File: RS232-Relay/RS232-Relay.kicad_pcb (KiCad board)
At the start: 2 copper layers, 82.5 x 151 mm, 133 parts, among them J10 Relay 1-4, J11 Relay 1-4, J2 Conn_01x02, J4 Conn_01x09, J5 Conn_01x09, J7 RS232_1, J8 RS232_2, J9 Relay 1-4, K1 G5V-1, K10 G5V-1, K11 G5V-1, K12 G5V-1, K2 G5V-1, K3 G5V-1, K4 G5V-1, K5 G5V-1, K6 G5V-1, K7 G5V-1, K8 G5V-1, K9 G5V-1, Q1 2N3904, Q10 2N3904, Q11 2N3904, Q12 2N3904, Q2 2N3904, Q3 2N3904, Q4 2N3904, Q5 2N3904, Q6 2N3904, Q7 2N3904, Q8 2N3904, Q9 2N3904, SW2 SW_SPST, SW3 SW_SPST, U1 TEC2-1210WI, U2 LTV-847S, U3 PCF8575DBR, U4 MAX3232, U6 LTV-847S, U7 LTV-847S

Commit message: 1x Layout Complete
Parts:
- removed D22, D23, D26, D27: 1N4148W, Diode_SMD:D_SOD-123
- removed D24, D25: RED, LED_SMD:LED_0805_2012Metric
- removed K10, K11, K12: G5V-1, Relay_THT:Relay_SPDT_Omron_G5V-1
- removed Q10, Q11, Q12: 2N3904, Package_TO_SOT_SMD:SOT-23
- removed R35, R40, R41: 220R, Resistor_SMD:R_0603_1608Metric
- removed R36, R37, R42, R43: 660R, Resistor_SMD:R_0603_1608Metric
- removed R38, R39: 1000R, Resistor_SMD:R_0603_1608Metric
- removed U7: LTV-847S, Package_DIP:SMDIP-16_W9.53mm
- added D28: RED, LED_SMD:LED_0805_2012Metric, F.Cu at (103.4, 39.6)
- added D29: 1N4148W, Diode_SMD:D_SOD-123, F.Cu at (103.0, 43.1)
- added D30: RED, LED_SMD:LED_0805_2012Metric, F.Cu at (53.7, 145.8)
- added D31: 1N4148W, Diode_SMD:D_SOD-123, F.Cu at (53.3, 149.3)
- added D32: RED, LED_SMD:LED_0805_2012Metric, F.Cu at (55.0, 92.4)
- added D33: 1N4148W, Diode_SMD:D_SOD-123, F.Cu at (54.6, 95.9)
- added K13: G5V-1, Relay_THT:Relay_SPDT_Omron_G5V-1, F.Cu at (99.9, 40.4)
- added K14: G5V-1, Relay_THT:Relay_SPDT_Omron_G5V-1, F.Cu at (50.2, 146.6)
- added K15: G5V-1, Relay_THT:Relay_SPDT_Omron_G5V-1, F.Cu at (51.5, 93.3)
- added Q13: 2N3904, Package_TO_SOT_SMD:SOT-23, F.Cu at (106.7, 44.4)
- added Q14: 2N3904, Package_TO_SOT_SMD:SOT-23, F.Cu at (57.0, 150.6)
- added Q15: 2N3904, Package_TO_SOT_SMD:SOT-23, F.Cu at (58.3, 97.2)
- added R44: 1000R, Resistor_SMD:R_0603_1608Metric, F.Cu at (106.9, 39.6)
- added R45: 220R, Resistor_SMD:R_0603_1608Metric, F.Cu at (116.5, 71.8)
- added R46: 660R, Resistor_SMD:R_0603_1608Metric, F.Cu at (107.0, 41.6)
- added R47: 1000R, Resistor_SMD:R_0603_1608Metric, F.Cu at (57.2, 145.8)
- added R48: 220R, Resistor_SMD:R_0603_1608Metric, F.Cu at (61.4, 147.8)
- added R49: 660R, Resistor_SMD:R_0603_1608Metric, F.Cu at (57.2, 147.8)
- added R50: 1000R, Resistor_SMD:R_0603_1608Metric, F.Cu at (58.5, 92.4)
- added R51: 220R, Resistor_SMD:R_0603_1608Metric, F.Cu at (62.7, 94.4)
- added R52: 660R, Resistor_SMD:R_0603_1608Metric, F.Cu at (58.5, 94.4)
- added U5: LTV-847S, Package_DIP:SMDIP-16_W9.53mm, F.Cu at (25.8, 163.1)
- D13, D17, D21: value RED -> 1N4148W; footprint LED_SMD:LED_0805_2012Metric -> Diode_SMD:D_SOD-123
- D14, D18: value 1N4148W -> RED; footprint Diode_SMD:D_SOD-123 -> LED_SMD:LED_0805_2012Metric
- R22, R34: value 1000R -> 660R
- R23, R29: value 220R -> 1000R
- R24, R30: value 660R -> 220R
- R27: value 1000R -> 220R
- R28: value 220R -> 660R
- moved Q7 183.9 mm to (106.9, 75.0), turned to 180 degrees
- moved K5 182.3 mm to (50.6, 167.5), turned to -90 degrees
- moved R27 180.1 mm to (121.8, 71.8), turned to -90 degrees
- moved K7 173.3 mm to (100.1, 71.0), turned to -90 degrees
- moved Q5 170.6 mm to (57.4, 171.4), turned to 180 degrees
- moved D16 170.1 mm to (103.6, 70.2), turned to 180 degrees
- moved D17 169.7 mm to (103.1, 73.7), turned to -90 degrees
- moved K8 169.7 mm to (50.7, 177.8), turned to -90 degrees
- moved Q8 168.6 mm to (57.5, 181.8), turned to 180 degrees
- moved R26 165.4 mm to (107.0, 70.2)
- moved D18 163.7 mm to (54.2, 177.0), turned to 180 degrees
- moved D19 163.5 mm to (53.8, 180.5), turned to -90 degrees
- moved R28 161.6 mm to (107.1, 72.2), turned to 180 degrees
- moved R21 159.9 mm to (61.7, 168.7), turned to 90 degrees
- moved R30 159.2 mm to (61.9, 179.0), turned to 90 degrees
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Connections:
- net Net-(R25-Pad1) renamed /Relay-Module2/Relay-NO-ISO2/OPTO_RIGHT_OUT
- D13 pad 1: Net-(D13-K) -> +12V
- D13 pad 2: +12V -> Net-(D13-A)
- D14 pad 1: +12V -> Net-(D14-K)
- D14 pad 2: Net-(D14-A) -> +12V
- D17 pad 1: Net-(D17-K) -> +12V
- D17 pad 2: +12V -> Net-(D17-A)
- D18 pad 1: +12V -> Net-(D18-K)
- D18 pad 2: Net-(D18-A) -> +12V
- D21 pad 1: Net-(D21-K) -> +12V
- D21 pad 2: +12V -> Net-(D21-A)
- K1 pad 5: /Relay-Module/RELAY_OUT_03 -> /Relay-Module/RELAY_OUT_02
- K1 pad 6: /Relay-Module/RELAY_OUT_03 -> /Relay-Module/RELAY_OUT_02
- K2 pad 5: /Relay-Module/RELAY_OUT_01 -> /Relay-Module1/RELAY_OUT_02
- K2 pad 6: /Relay-Module/RELAY_OUT_01 -> /Relay-Module1/RELAY_OUT_02
- K3 pad 5: /Relay-Module/RELAY_OUT_02 -> /Relay-Module2/RELAY_OUT_02
- K3 pad 6: /Relay-Module/RELAY_OUT_02 -> /Relay-Module2/RELAY_OUT_02
- K4 pad 5: /Relay-Module/RELAY_OUT_04 -> /Relay-Module/RELAY_OUT_03
- K4 pad 6: /Relay-Module/RELAY_OUT_04 -> /Relay-Module/RELAY_OUT_03
- K5 pad 5: /Relay-Module1/RELAY_OUT_01 -> /Relay-Module1/RELAY_OUT_03
- K5 pad 6: /Relay-Module1/RELAY_OUT_01 -> /Relay-Module1/RELAY_OUT_03
- K5 pad 9: Net-(D14-A) -> Net-(D13-A)
- K6 pad 5: /Relay-Module1/RELAY_OUT_03 -> /Relay-Module2/RELAY_OUT_03
- K6 pad 6: /Relay-Module1/RELAY_OUT_03 -> /Relay-Module2/RELAY_OUT_03
- K7 pad 5: /Relay-Module1/RELAY_OUT_04 -> /Relay-Module/RELAY_OUT_04
- K7 pad 6: /Relay-Module1/RELAY_OUT_04 -> /Relay-Module/RELAY_OUT_04
- K7 pad 9: Net-(D18-A) -> Net-(D17-A)
- K8 pad 5: /Relay-Module1/RELAY_OUT_02 -> /Relay-Module1/RELAY_OUT_04
- K8 pad 6: /Relay-Module1/RELAY_OUT_02 -> /Relay-Module1/RELAY_OUT_04
- K9 pad 5: /Relay-Module2/RELAY_OUT_01 -> /Relay-Module2/RELAY_OUT_04
- K9 pad 6: /Relay-Module2/RELAY_OUT_01 -> /Relay-Module2/RELAY_OUT_04
- K9 pad 9: Net-(D22-A) -> Net-(D21-A)
- Q5 pad 3: Net-(D14-A) -> Net-(D13-A)
- Q7 pad 3: Net-(D18-A) -> Net-(D17-A)
- Q9 pad 3: Net-(D22-A) -> Net-(D21-A)
- R12 pad 1: Net-(R12-Pad1) -> /Relay-Module1/Relay-NO-ISO1/OPTO_LEFT_IN
- R12 pad 2: RELAY_IN_01 -> RELAY_IN_06
- R13 pad 1: Net-(R13-Pad1) -> /Relay-Module1/Relay-NO-ISO1/OPTO_RIGHT_OUT
- R15 pad 1: Net-(R15-Pad1) -> /Relay-Module2/Relay-NO-ISO1/OPTO_LEFT_IN
- R15 pad 2: RELAY_IN_02 -> RELAY_IN_10
- R16 pad 1: Net-(R16-Pad1) -> /Relay-Module2/Relay-NO-ISO1/OPTO_RIGHT_OUT
- R18 pad 1: Net-(R18-Pad1) -> /Relay-Module/Relay-NO-ISO2/OPTO_LEFT_IN
- R18 pad 2: RELAY_IN_04 -> RELAY_IN_03
- R19 pad 1: Net-(R19-Pad1) -> /Relay-Module/Relay-NO-ISO2/OPTO_RIGHT_OUT
- R20 pad 2: Net-(D14-A) -> Net-(D13-A)
- R21 pad 1: Net-(R21-Pad1) -> /Relay-Module1/Relay-NO-ISO2/OPTO_LEFT_IN
- R21 pad 2: RELAY_IN_05 -> RELAY_IN_07
- R22 pad 1: Net-(D13-K) -> /Relay-Module1/Relay-NO-ISO2/OPTO_RIGHT_OUT
- R22 pad 2: Net-(D15-A) -> Net-(Q5-B)
- R23 pad 1: Net-(R23-Pad1) -> Net-(D14-K)
- R23 pad 2: RELAY_IN_07 -> Net-(D15-A)
- R24 pad 1: Net-(R24-Pad1) -> /Relay-Module2/Relay-NO-ISO2/OPTO_LEFT_IN
- R24 pad 2: Net-(Q5-B) -> RELAY_IN_11
- R26 pad 2: Net-(D18-A) -> Net-(D17-A)
- R27 pad 1: Net-(D17-K) -> /Relay-Module/Relay-NO-ISO3/OPTO_LEFT_IN
- R27 pad 2: Net-(D19-A) -> RELAY_IN_04
- R28 pad 1: Net-(R28-Pad1) -> /Relay-Module/Relay-NO-ISO3/OPTO_RIGHT_OUT
- R28 pad 2: RELAY_IN_08 -> Net-(Q7-B)
- R29 pad 1: Net-(R29-Pad1) -> Net-(D18-K)
- R29 pad 2: RELAY_IN_06 -> Net-(D19-A)
- R3 pad 1: Net-(R3-Pad1) -> /Relay-Module/Relay-NO-ISO1/OPTO_LEFT_IN
- R3 pad 2: RELAY_IN_03 -> RELAY_IN_02
- R30 pad 1: Net-(R30-Pad1) -> /Relay-Module1/Relay-NO-ISO3/OPTO_LEFT_IN
- R30 pad 2: Net-(Q7-B) -> RELAY_IN_08
- R31 pad 1: Net-(R31-Pad1) -> /Relay-Module1/Relay-NO-ISO3/OPTO_RIGHT_OUT
- R32 pad 2: Net-(D22-A) -> Net-(D21-A)
- R33 pad 1: Net-(R33-Pad1) -> /Relay-Module2/Relay-NO-ISO3/OPTO_LEFT_IN
- R33 pad 2: RELAY_IN_09 -> RELAY_IN_12
- R34 pad 1: Net-(D21-K) -> /Relay-Module2/Relay-NO-ISO3/OPTO_RIGHT_OUT
- R34 pad 2: Net-(D23-A) -> Net-(Q9-B)
- R5 pad 1: Net-(R5-Pad1) -> /Relay-Module/Relay-NO-ISO1/OPTO_RIGHT_OUT
- U2 pad 1: Net-(R12-Pad1) -> /Relay-Module/Relay-NO-ISO3/OPTO_LEFT_IN
- U2 pad 11: Net-(R5-Pad1) -> /Relay-Module/Relay-NO-ISO2/OPTO_RIGHT_OUT
- U2 pad 13: Net-(R16-Pad1) -> /Relay-Module/Relay-NO-ISO1/OPTO_RIGHT_OUT
- U2 pad 15: Net-(R13-Pad1) -> /Relay-Module/Relay-NO-ISO3/OPTO_RIGHT_OUT
- U2 pad 3: Net-(R15-Pad1) -> /Relay-Module/Relay-NO-ISO1/OPTO_LEFT_IN
- U2 pad 5: Net-(R3-Pad1) -> /Relay-Module/Relay-NO-ISO2/OPTO_LEFT_IN
- U2 pad 7: Net-(R18-Pad1) -> /Relay-Module/Relay-NO-ISO/OPTO_LEFT_IN
- U2 pad 9: Net-(R19-Pad1) -> /Relay-Module/Relay-NO-ISO/OPTO_RIGHT_OUT
- U6 pad 1: Net-(R21-Pad1) -> /Relay-Module2/Relay-NO-ISO3/OPTO_LEFT_IN
- U6 pad 13: Net-(R31-Pad1) -> /Relay-Module2/Relay-NO-ISO1/OPTO_RIGHT_OUT
- U6 pad 15: Net-(R24-Pad1) -> /Relay-Module2/Relay-NO-ISO3/OPTO_RIGHT_OUT
- U6 pad 3: Net-(R29-Pad1) -> /Relay-Module2/Relay-NO-ISO1/OPTO_LEFT_IN
- U6 pad 5: Net-(R23-Pad1) -> /Relay-Module2/Relay-NO-ISO2/OPTO_LEFT_IN
- U6 pad 7: Net-(R28-Pad1) -> /Relay-Module2/Relay-NO-ISO/OPTO_LEFT_IN
- U6 pad 9: Net-(R30-Pad1) -> /Relay-Module2/Relay-NO-ISO/OPTO_RIGHT_OUT
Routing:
- net +12V: track 32.6 -> 152.9 mm
- net /Relay-Module/Relay-NO-ISO/OPTO_LEFT_IN: track 0.00 -> 23.0 mm
- net GND: track 1.93 -> 21.3 mm, vias 1 -> 12
- net Net-(D29-A): track 0.00 -> 17.6 mm
- net Net-(D4-A): track 0.00 -> 17.6 mm
- net Net-(D15-A): track 0.00 -> 17.6 mm
- net Net-(D31-A): track 0.00 -> 17.6 mm
- net Net-(D19-A): track 0.00 -> 17.6 mm
- net Net-(D9-A): track 0.00 -> 17.6 mm
- net Net-(D17-A): track 0.00 -> 17.6 mm
- net Net-(D13-A): track 0.00 -> 17.6 mm
- net Net-(D11-A): track 0.00 -> 17.6 mm
- net Net-(D33-A): track 0.00 -> 17.6 mm
- net Net-(D21-A): track 0.00 -> 17.6 mm
- net /Relay-Module/Relay-NO-ISO2/OPTO_LEFT_IN: track 0.00 -> 16.0 mm
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
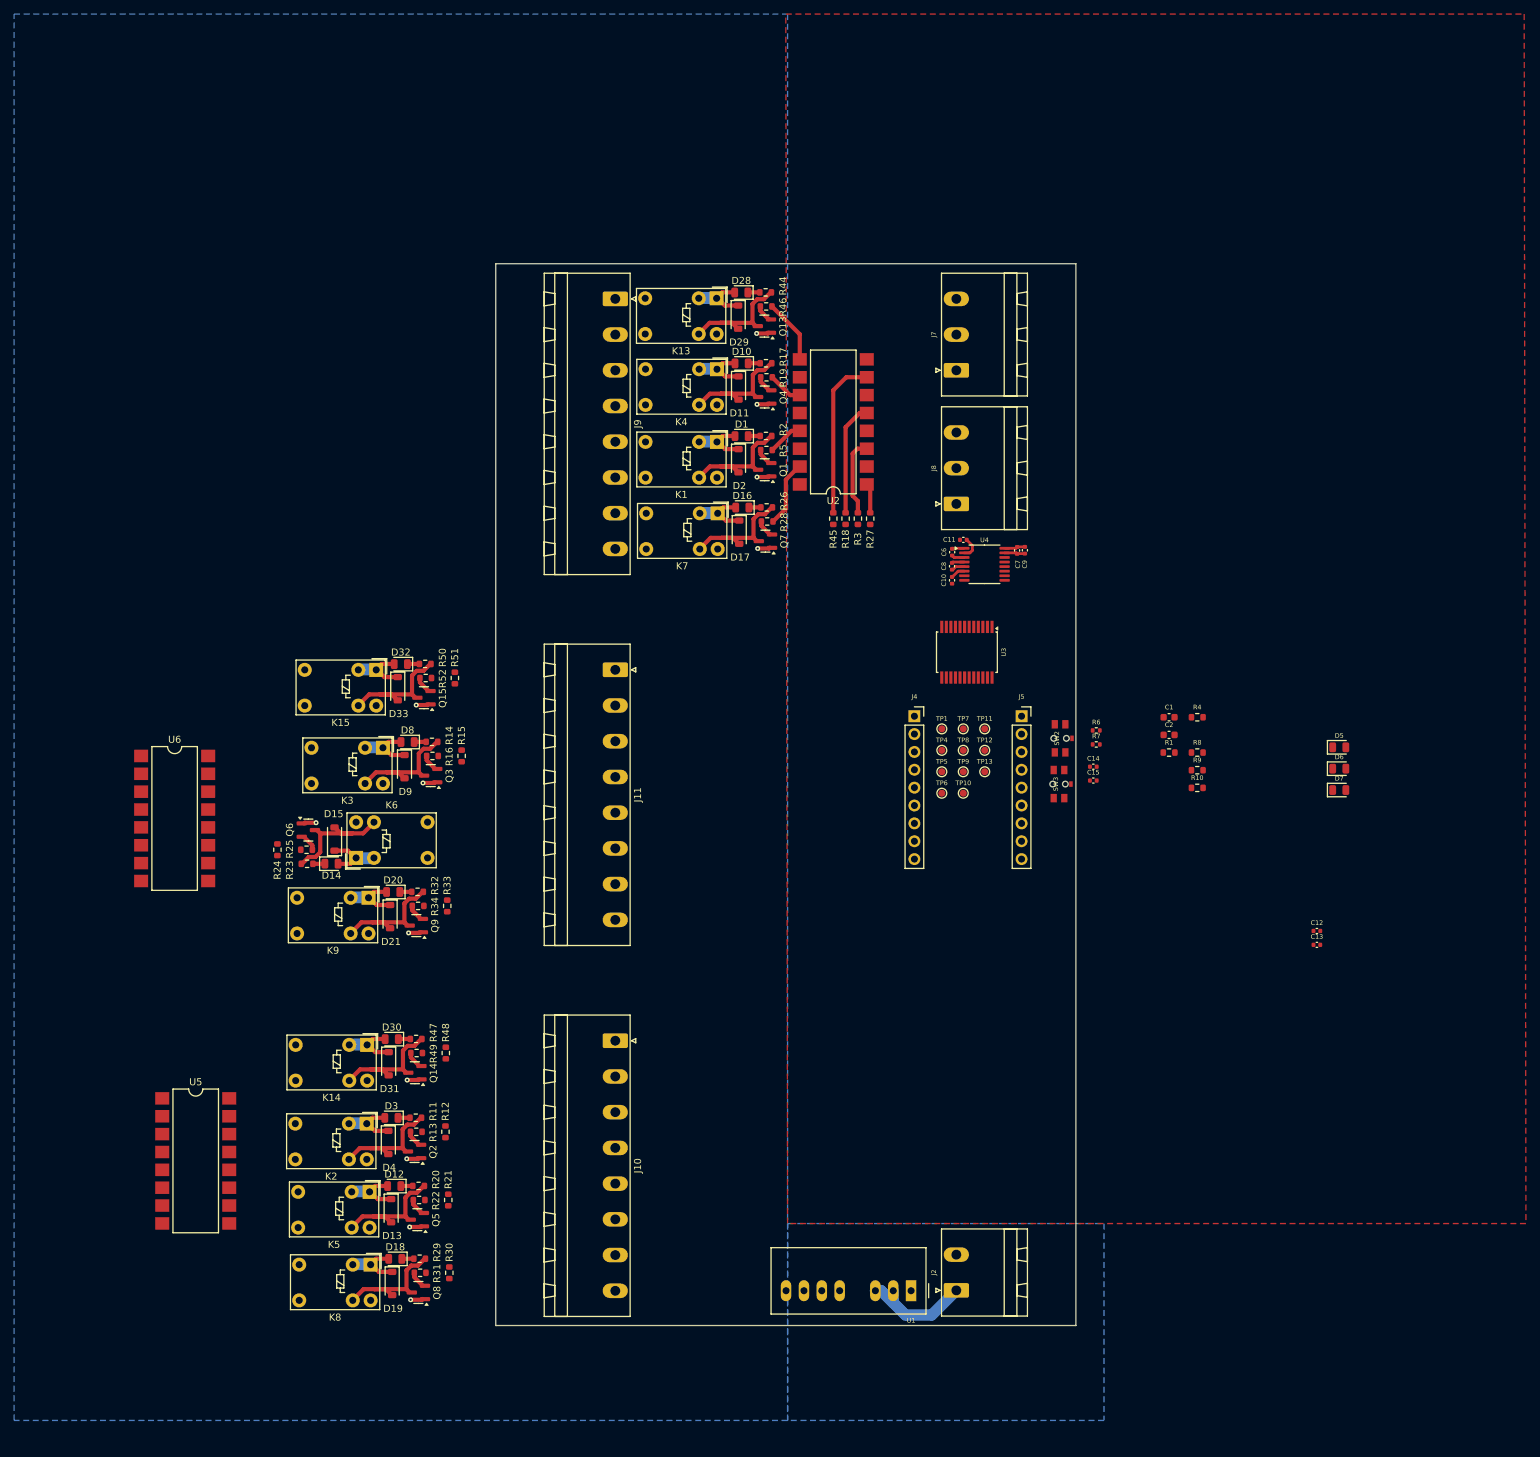
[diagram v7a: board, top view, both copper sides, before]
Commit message: Routing Complete (vias next)
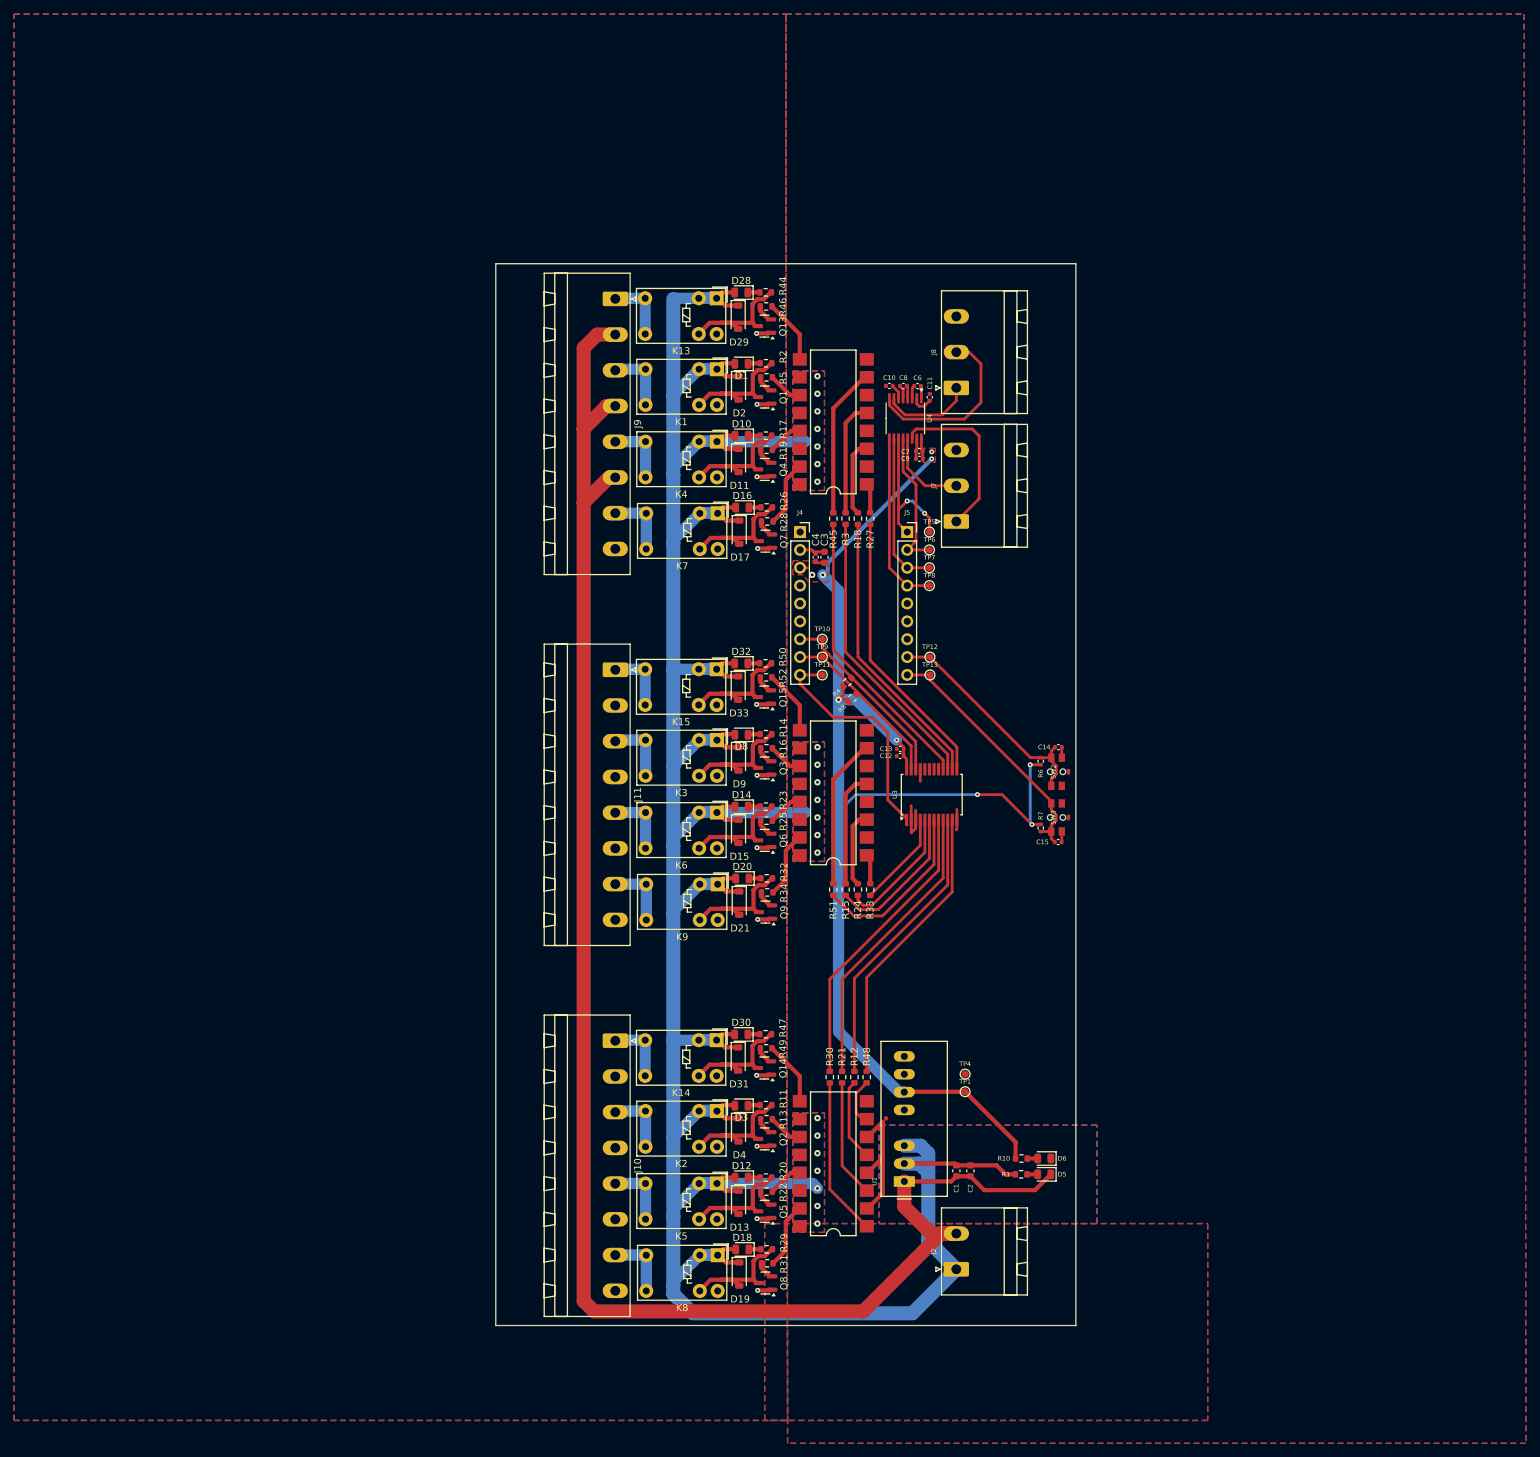
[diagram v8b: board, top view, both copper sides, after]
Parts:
- removed D7: Green, LED_SMD:LED_0805_2012Metric
- removed R9: 220R, Resistor_SMD:R_0603_1608Metric
- added C3: 10u, Capacitor_SMD:C_0603_1608Metric, F.Cu at (115.2, 77.2)
- added C4: 1uF, Capacitor_SMD:C_0402_1005Metric, F.Cu at (114.0, 77.2)
- moved U6 93.7 mm to (116.5, 110.8), turned to 180 degrees
- moved U5 90.7 mm to (116.5, 163.5), turned to 180 degrees
- moved R24 82.7 mm to (120.0, 124.5)
- moved D5 73.8 mm to (146.5, 165.0), turned to 180 degrees
- moved C1 71.2 mm to (134.0, 164.5), turned to -90 degrees
- moved D6 69.5 mm to (146.5, 162.8), turned to 180 degrees
- moved C2 68.1 mm to (136.0, 164.5), turned to -90 degrees
- moved R23 65.8 mm to (106.9, 112.7), turned to 0 degrees
- moved R25 65.5 mm to (107.0, 114.7), turned to 180 degrees
- moved C13 65.5 mm to (126.0, 104.5)
- moved Q6 64.9 mm to (106.8, 117.5), turned to 180 degrees
- moved C12 64.3 mm to (126.0, 105.5)
- moved R1 63.6 mm to (143.2, 165.0)
- moved R51 61.6 mm to (116.5, 124.5), turned to -90 degrees
- moved R30 60.8 mm to (116.0, 151.2)
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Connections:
- J4 pad 7: I2C_SDA -> I2C_SCL
- J4 pad 8: I2C_SCL -> I2C_SDA
- U2 pad 11: /Relay-Module/Relay-NO-ISO2/OPTO_RIGHT_OUT -> /Relay-Module/Relay-NO-ISO1/OPTO_RIGHT_OUT
- U2 pad 13: /Relay-Module/Relay-NO-ISO1/OPTO_RIGHT_OUT -> /Relay-Module/Relay-NO-ISO2/OPTO_RIGHT_OUT
- U2 pad 3: /Relay-Module/Relay-NO-ISO1/OPTO_LEFT_IN -> /Relay-Module/Relay-NO-ISO2/OPTO_LEFT_IN
- U2 pad 5: /Relay-Module/Relay-NO-ISO2/OPTO_LEFT_IN -> /Relay-Module/Relay-NO-ISO1/OPTO_LEFT_IN
- U3 pad 10: RELAY_IN_07 -> RELAY_IN_06
- U3 pad 11: RELAY_IN_08 -> RELAY_IN_05
- U3 pad 13: RELAY_IN_09 -> RELAY_IN_04
- U3 pad 14: RELAY_IN_10 -> RELAY_IN_03
- U3 pad 15: RELAY_IN_11 -> RELAY_IN_02
- U3 pad 16: RELAY_IN_12 -> RELAY_IN_01
- U3 pad 4: RELAY_IN_01 -> RELAY_IN_12
- U3 pad 5: RELAY_IN_02 -> RELAY_IN_11
- U3 pad 6: RELAY_IN_03 -> RELAY_IN_10
- U3 pad 7: RELAY_IN_04 -> RELAY_IN_09
- U3 pad 8: RELAY_IN_05 -> RELAY_IN_08
- U3 pad 9: RELAY_IN_06 -> RELAY_IN_07
- U5 pad 11: /Relay-Module1/Relay-NO-ISO2/OPTO_RIGHT_OUT -> /Relay-Module1/Relay-NO-ISO1/OPTO_RIGHT_OUT
- U5 pad 13: /Relay-Module1/Relay-NO-ISO1/OPTO_RIGHT_OUT -> /Relay-Module1/Relay-NO-ISO2/OPTO_RIGHT_OUT
- U5 pad 3: /Relay-Module1/Relay-NO-ISO1/OPTO_LEFT_IN -> /Relay-Module1/Relay-NO-ISO2/OPTO_LEFT_IN
- U5 pad 5: /Relay-Module1/Relay-NO-ISO2/OPTO_LEFT_IN -> /Relay-Module1/Relay-NO-ISO1/OPTO_LEFT_IN
- U6 pad 11: /Relay-Module2/Relay-NO-ISO2/OPTO_RIGHT_OUT -> /Relay-Module2/Relay-NO-ISO1/OPTO_RIGHT_OUT
- U6 pad 13: /Relay-Module2/Relay-NO-ISO1/OPTO_RIGHT_OUT -> /Relay-Module2/Relay-NO-ISO2/OPTO_RIGHT_OUT
- U6 pad 3: /Relay-Module2/Relay-NO-ISO1/OPTO_LEFT_IN -> /Relay-Module2/Relay-NO-ISO2/OPTO_LEFT_IN
- U6 pad 5: /Relay-Module2/Relay-NO-ISO2/OPTO_LEFT_IN -> /Relay-Module2/Relay-NO-ISO1/OPTO_LEFT_IN
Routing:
- net +12V: track 152.9 -> 467.1 mm, vias 0 -> 21
- net GND: track 21.3 -> 267.6 mm
- net +3V3: track 2.97 -> 191.4 mm, vias 0 -> 9
- net RELAY_IN_08: track 0.00 -> 42.2 mm
- net RELAY_IN_07: track 0.00 -> 41.7 mm
- net RELAY_IN_01: track 0.00 -> 41.3 mm
- net RELAY_IN_06: track 0.00 -> 41.2 mm
- net RELAY_IN_02: track 0.00 -> 40.8 mm
- net RELAY_IN_05: track 0.00 -> 40.8 mm
- net RELAY_IN_03: track 0.00 -> 40.4 mm
- net RELAY_IN_04: track 0.00 -> 39.9 mm
- net GNDREF: track 2.95 -> 41.8 mm
- net BTN_02: track 0.00 -> 36.4 mm
- net I2C_INT: track 0.00 -> 33.3 mm
- net BTN_01: track 0.00 -> 32.7 mm
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- added copper zone on B.Cu, net +12V
- added copper zone on F.Cu, net +12V
- added copper zone on F.Cu, net +3V3
- added copper zone on F.Cu, net GND
